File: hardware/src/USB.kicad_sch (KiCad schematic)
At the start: 0 parts

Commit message: Add: USB sheet to the schematic
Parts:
- added C301: 10nF, symbol Device:C
- added C302, C303, C304: 4.7µF, symbol Device:C
- added C305, C306, C307: 0.1µF, symbol Device:C
- added D301: SP0503BAHT, Package_TO_SOT_SMD:SOT-143, symbol Power_Protection:SP0503BAHT
- added D302, D303: LED, symbol Device:LED
- added J301: USB_C_Receptacle_USB2.0_16P, Connector_USB:USB_C_Receptacle_GCT_USB4105-xx-A_16P_TopMnt_Horizontal, symbol Connector:USB_C_Receptacle_USB2.0_16P
- added Q301, Q302: NPN, symbol Simulation_SPICE:NPN
- added R301: 0R, symbol Device:R
- added R302, R303: 5.1k, symbol Device:R
- added R304: 22.1k, symbol Device:R
- added R305: 47.5k, symbol Device:R
- added R306: 1k, symbol Device:R
- added R307, R308: 10k, symbol Device:R
- added R309, R310: 150, symbol Device:R
- added U301: CP2102N-Axx-xQFN24, Package_DFN_QFN:QFN-24-1EP_4x4mm_P0.5mm_EP2.6x2.6mm, symbol Interface_USB:CP2102N-Axx-xQFN24
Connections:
- new net: Q301.2 (B), R307.1
- new net: Q302.3 (E), R307.2, U301.19 (~{RTS})
- new net: D303.1 (K), U301.13 (~{RXT}/GPIO.1)
- new net: D303.2 (A), R310.2
- new net: Q301.3 (E), R308.2, U301.23 (~{DTR})
- new net: D302.1 (K), U301.14 (~{TXT}/GPIO.0)
- new net: D301.4 (K), J301.A6 (D+), J301.B6 (D+), U301.3 (D+)
- new net: D301.3 (K), J301.A7 (D-), J301.B7 (D-), U301.4 (D-)
- new net: R304.2, R305.1, U301.8 (VBUS)
- new net: R306.2, U301.9 (~{RST})
- new net: J301.A5 (CC1), R302.2
- new net: C301.1, J301.S1 (SHIELD), R301.1
- new net: Q302.2 (B), R308.1
- new net: J301.B5 (CC2), R303.2
- new net: D302.2 (A), R309.2
- new net +3V3: C302.1, C303.1, C304.1, C305.1, C306.1, C307.1, R306.1, R309.1, R310.1, U301.5 (VIO), U301.6 (VDD), U301.7 (VREGIN)
- new net GND: C301.2, C302.2, C303.2, C304.2, C305.2, C306.2, C307.2, D301.1 (A), J301.A1 (GND), J301.A12 (GND), J301.B1 (GND), J301.B12 (GND), R301.2, R302.1, R303.1, R305.2, U301.2 (GND), U301.25 (GND)
- new net GPIO9: Q301.1 (C)
- new net RST: Q302.1 (C)
- new net RXD: U301.20 (RXD)
- new net TXD: U301.21 (TXD)
- new net VBUS: D301.2 (K), J301.A4 (VBUS), J301.A9 (VBUS), J301.B4 (VBUS), J301.B9 (VBUS), R304.1
- no-connect marks 0 -> 8

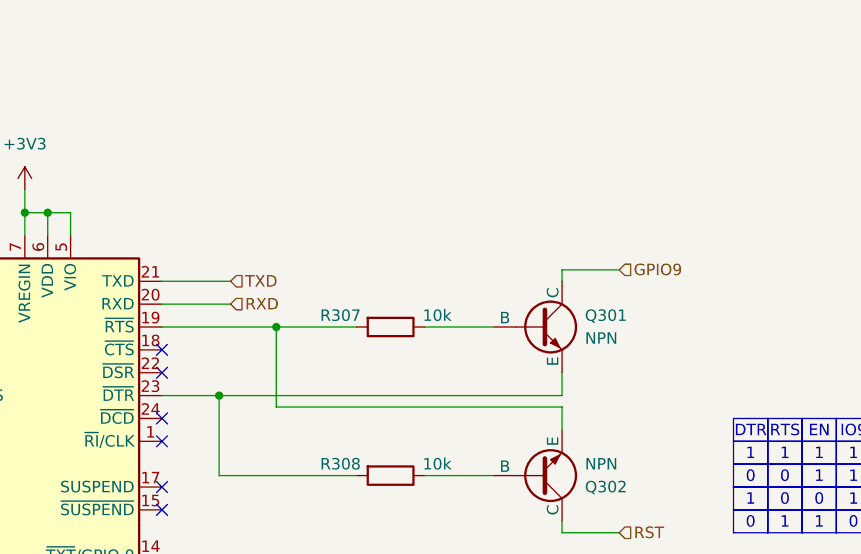
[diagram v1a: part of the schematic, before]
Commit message: Mod: Compacted the TXD and RXD into the UART bus
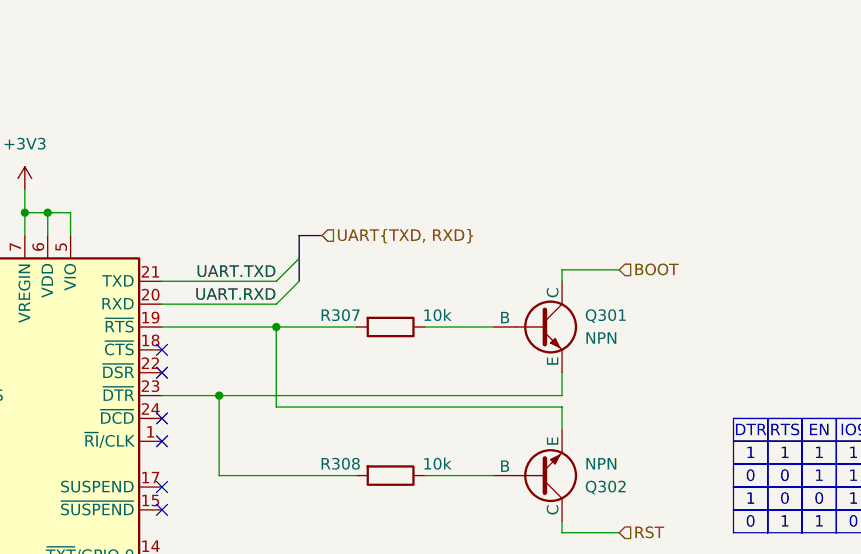
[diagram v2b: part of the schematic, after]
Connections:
- net GPIO9 renamed BOOT
- net RXD renamed UART.RXD
- net TXD renamed UART.TXD
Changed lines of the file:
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@@
 	(title_block
 		(title "Wordclock - USB")
-		(date "2024-10-19")
+		(date "2024-10-20")
 		(rev "A")
 		(company "ElektroNik Zoller")
@@
 		(at 165.1 104.14)
 	)
+	(bus_entry
+		(at 177.8 68.58)
+		(size 2.54 -2.54)
+		(stroke
+			(width 0)
+			(type default)
+		)
+	)
+	(bus_entry
+		(at 177.8 66.04)
+		(size 2.54 -2.54)
+		(stroke
+			(width 0)
+			(type default)
+		)
+	)
+	(bus
+		(pts
+			(xy 180.34 63.5) (xy 180.34 60.96)
+		)
+		(stroke
+			(width 0)
+			(type default)
+		)
+	)
 	(wire
 		(pts
@@
 	(wire
 		(pts
-			(xy 165.1 68.58) (xy 172.72 68.58)
+			(xy 165.1 68.58) (xy 177.8 68.58)
 		)
 		(stroke
@@
 		)
 	)
+	(bus
+		(pts
+			(xy 180.34 60.96) (xy 182.88 60.96)
+		)
+		(stroke
+			(width 0)
+			(type default)
+		)
+	)
 	(wire
 		(pts
@@
 	(wire
 		(pts
-			(xy 165.1 66.04) (xy 172.72 66.04)
+			(xy 165.1 66.04) (xy 177.8 66.04)
 		)
 		(stroke
@@
 		(pts
 			(xy 97.79 83.82) (xy 139.7 83.82)
+		)
+		(stroke
+			(width 0)
+			(type default)
+		)
+	)
+	(bus
+		(pts
+			(xy 180.34 66.04) (xy 180.34 63.5)
 		)
 		(stroke
@@
 		)
 	)
-	(hierarchical_label "GPIO9"
+	(label "UART.RXD"
+		(at 177.8 68.58 180)
+		(fields_autoplaced yes)
+		(effects
+			(font
+				(size 1.27 1.27)
+			)
+			(justify right bottom)
+		)
+	)
+	(label "UART.TXD"
+		(at 177.8 66.04 180)
+		(fields_autoplaced yes)
+		(effects
+			(font
+				(size 1.27 1.27)
+			)
+			(justify right bottom)
+		)
+	)
+	(hierarchical_label "BOOT"
 		(shape input)
 		(at 215.9 64.77 0)
-		(fields_autoplaced yes)
-		(effects
-			(font
-				(size 1.27 1.27)
-			)
-			(justify left)
-		)
-	)
-	(hierarchical_label "RXD"
-		(shape input)
-		(at 172.72 68.58 0)
 		(fields_autoplaced yes)
 		(effects
@@
 		)
 	)
-	(hierarchical_label "TXD"
+	(hierarchical_label "UART{TXD, RXD}"
 		(shape input)
-		(at 172.72 66.04 0)
+		(at 182.88 60.96 0)
 		(fields_autoplaced yes)
 		(effects

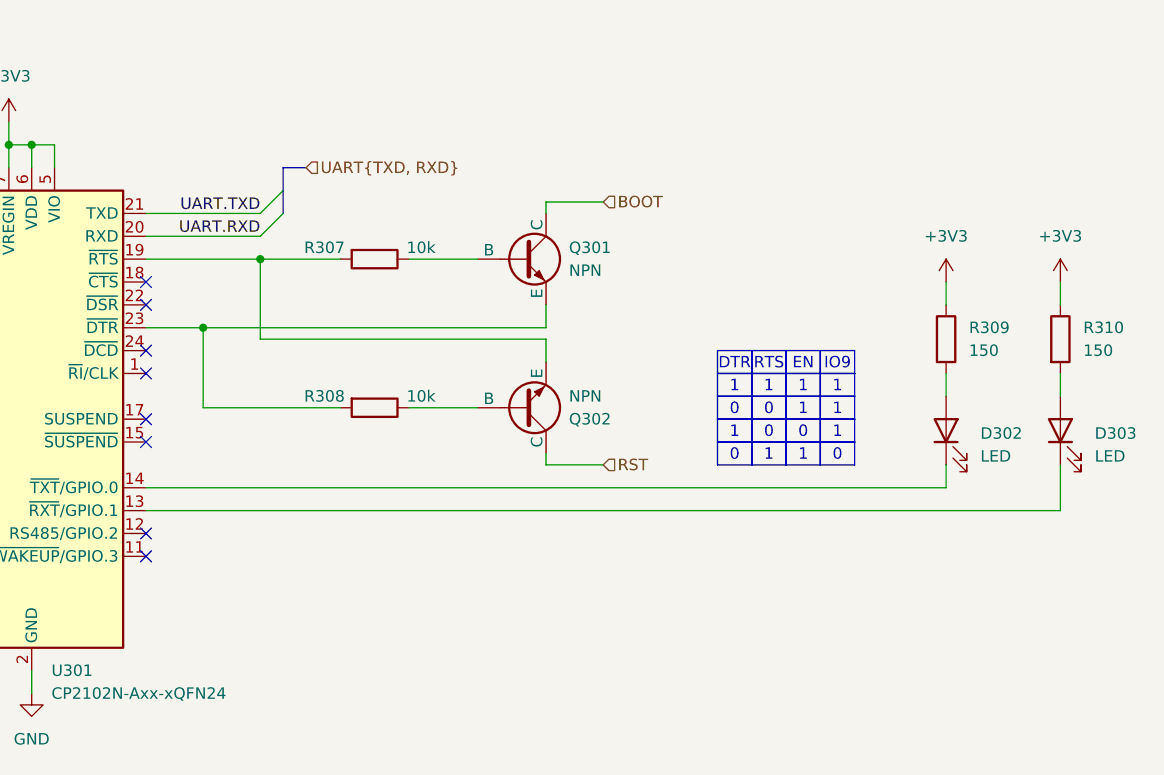
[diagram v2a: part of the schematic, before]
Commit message: Add: MCU and power supply. And connected to USB in top level schematic
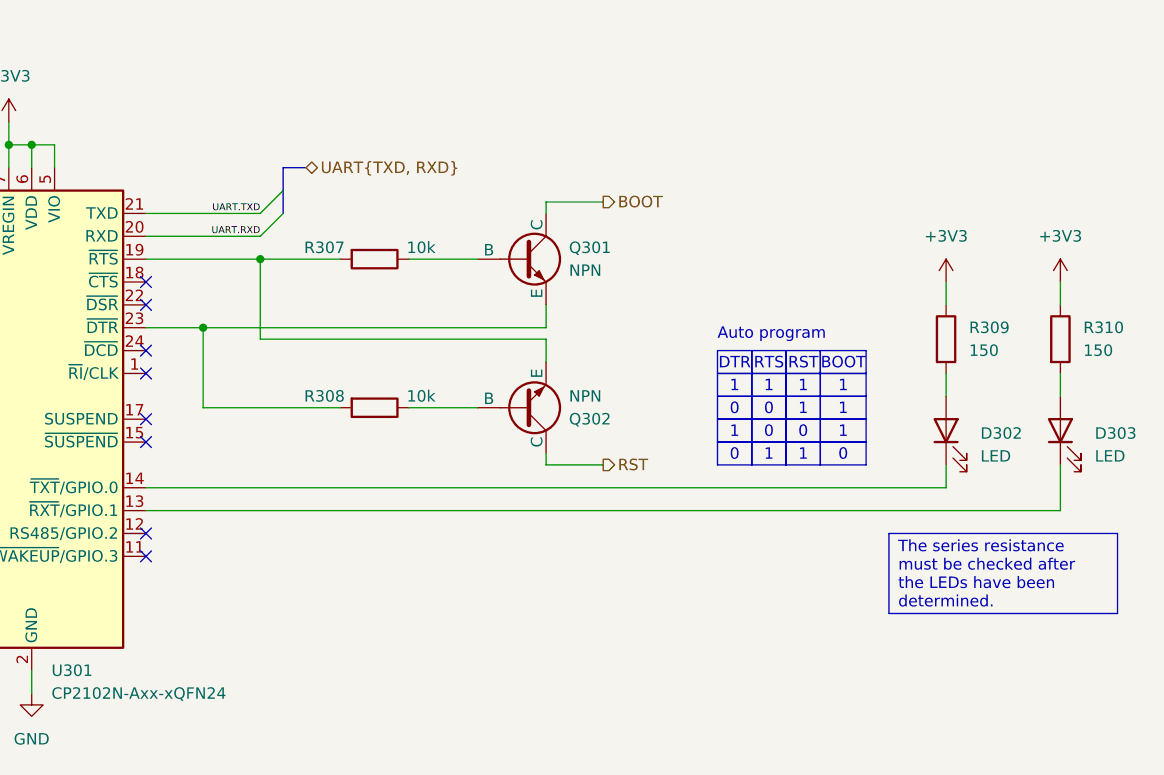
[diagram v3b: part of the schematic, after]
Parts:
- J301: Manufacturer (none) -> GCT; Manufacturer Part no. (none) -> USB4105-GF-A; Vendor 1 (none) -> Digikey; Vendor 1 Part no. (none) -> 2073-USB4105-GF-ACT-ND; Vendor 2 (none) -> LCSC; Vendor 2 Part no. (none) -> C3020560
- U301: Manufacturer (none) -> Silicon Labs; Manufacturer Part no. (none) -> CP2102N-A02-GQFN24R; Vendor 1 (none) -> Digikey; Vendor 1 Part no. (none) -> 336-5888-2-ND; Vendor 2 (none) -> LCSC; Vendor 2 Part no. (none) -> C969151
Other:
- note added: "Auto program"
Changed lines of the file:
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@@
 		(exclude_from_sim no)
 		(at 240.03 83.82 0)
-		(size 3.81 2.54)
+		(size 5.08 2.54)
+		(stroke
+			(width 0)
+			(type default)
+		)
+		(fill
+			(type none)
+		)
+		(effects
+			(font
+				(size 1.27 1.27)
+			)
+		)
+	)
+	(text_box "The series resistance must be checked after the LEDs have been determined."
+		(exclude_from_sim no)
+		(at 247.65 101.6 0)
+		(size 25.4 8.89)
 		(stroke
 			(width 0)
@@
 				(size 1.27 1.27)
 			)
+			(justify left)
 		)
 	)
@@
 		(exclude_from_sim no)
 		(at 240.03 86.36 0)
-		(size 3.81 2.54)
+		(size 5.08 2.54)
 		(stroke
 			(width 0)
@@
 		(exclude_from_sim no)
 		(at 240.03 88.9 0)
-		(size 3.81 2.54)
+		(size 5.08 2.54)
 		(stroke
 			(width 0)
@@
 		)
 	)
-	(text_box "EN"
+	(text_box "RST"
 		(exclude_from_sim no)
 		(at 236.22 81.28 0)
@@
 		(exclude_from_sim no)
 		(at 240.03 91.44 0)
-		(size 3.81 2.54)
+		(size 5.08 2.54)
 		(stroke
 			(width 0)
@@
 		)
 	)
-	(text_box "IO9"
+	(text_box "BOOT"
 		(exclude_from_sim no)
 		(at 240.03 81.28 0)
-		(size 3.81 2.54)
+		(size 5.08 2.54)
 		(stroke
 			(width 0)
@@
 		)
 	)
+	(text "Auto program"
+		(exclude_from_sim no)
+		(at 228.6 80.264 0)
+		(effects
+			(font
+				(size 1.27 1.27)
+			)
+			(justify left bottom)
+		)
+	)
 	(label "UART.RXD"
 		(at 177.8 68.58 180)
@@
 		(effects
 			(font
-				(size 1.27 1.27)
+				(size 0.762 0.762)
 			)
 			(justify right bottom)
@@
 		(effects
 			(font
-				(size 1.27 1.27)
+				(size 0.762 0.762)
 			)
 			(justify right bottom)
@@
 	)
 	(hierarchical_label "BOOT"
-		(shape input)
+		(shape output)
 		(at 215.9 64.77 0)
 		(fields_autoplaced yes)
@@
 	)
 	(hierarchical_label "RST"
-		(shape input)
+		(shape output)
 		(at 215.9 93.98 0)
 		(fields_autoplaced yes)
@@
 	)
 	(hierarchical_label "UART{TXD, RXD}"
-		(shape input)
+		(shape bidirectional)
 		(at 182.88 60.96 0)
 		(fields_autoplaced yes)
@@
 			)
 		)
+		(property "Manufacturer" "Silicon Labs"
+			(at 152.4 88.9 0)
+			(effects
+				(font
+					(size 1.27 1.27)
+				)
+				(hide yes)
+			)
+		)
+		(property "Manufacturer Part no." "CP2102N-A02-GQFN24R"
+			(at 152.4 88.9 0)
+			(effects
+				(font
+					(size 1.27 1.27)
+				)
+				(hide yes)
+			)
+		)
+		(property "Vendor 1" "Digikey"
+			(at 152.4 88.9 0)
+			(effects
+				(font
+					(size 1.27 1.27)
+				)
+				(hide yes)
+			)
+		)
+		(property "Vendor 1 Part no." "336-5888-2-ND"
+			(at 152.4 88.9 0)
+			(effects
+				(font
+					(size 1.27 1.27)
+				)
+				(hide yes)
+			)
+		)
+		(property "Vendor 2" "LCSC"
+			(at 152.4 88.9 0)
+			(effects
+				(font
+					(size 1.27 1.27)
+				)
+				(hide yes)
+			)
+		)
+		(property "Vendor 2 Part no." " C969151"
+			(at 152.4 88.9 0)
+			(effects
+				(font
+					(size 1.27 1.27)
+				)
+				(hide yes)
+			)
+		)
 		(pin "8"
 		)
@@
 			(at 50.8 81.28 0)
 			(effects
+				(font
+					(size 1.27 1.27)
+				)
+				(hide yes)
+			)
+		)
+		(property "Manufacturer" "GCT"
+			(at 50.8 81.28 0)
+			(effects
+				(font
+					(size 1.27 1.27)
+				)
+				(hide yes)
+			)
+		)
+		(property "Manufacturer Part no." "USB4105-GF-A"
+			(at 50.8 81.28 0)
+			(effects
+				(font
+					(size 1.27 1.27)
+				)
+				(hide yes)
+			)
+		)
+		(property "Vendor 1" "Digikey"
+			(at 50.8 81.28 0)
+			(effects
+				(font
+					(size 1.27 1.27)
+				)
+				(hide yes)
+			)
+		)
+		(property "Vendor 1 Part no." "2073-USB4105-GF-ACT-ND"
+			(at 50.8 81.28 0)
+			(effects
+				(font
+					(size 1.27 1.27)
+				)
+				(hide yes)
+			)
+		)
+		(property "Vendor 2" "LCSC"
+			(at 50.8 81.28 0)
+			(effects
+				(font
+					(size 1.27 1.27)
+				)
+				(hide yes)
+			)
+		)
+		(property "Vendor 2 Part no." " C3020560"
+			(at 50.8 81.28 0)
+			(effects

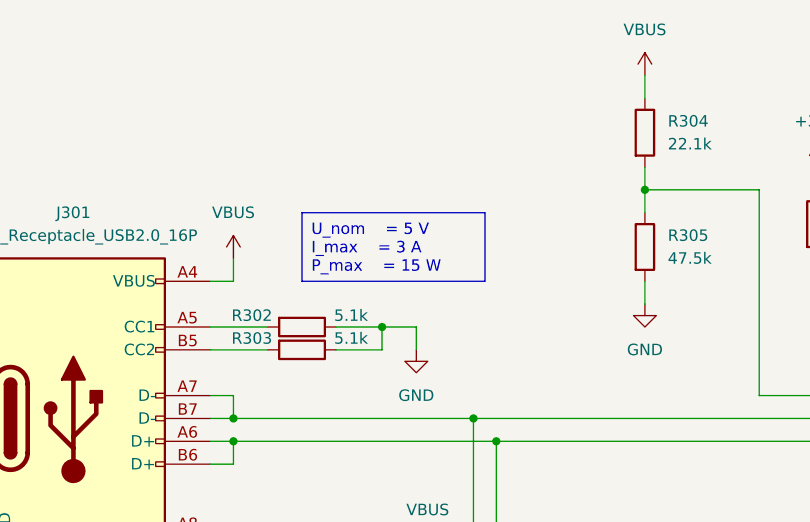
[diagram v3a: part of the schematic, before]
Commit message: Add: LEDs to the schematic
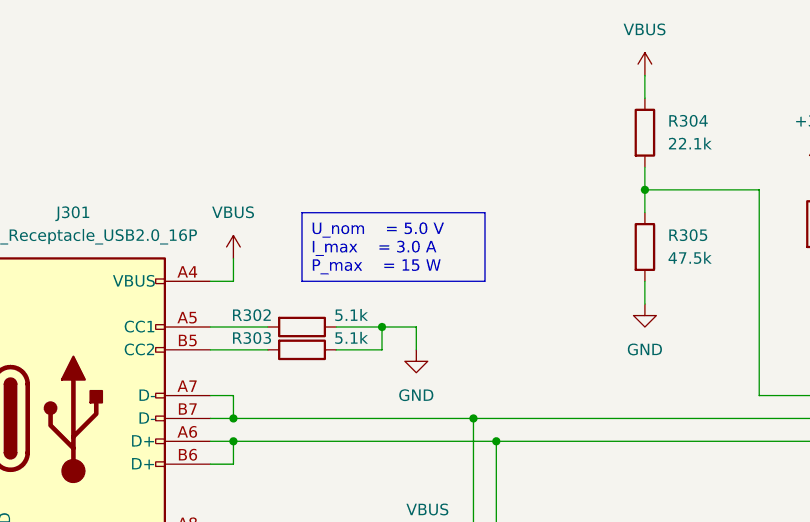
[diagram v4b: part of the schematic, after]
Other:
- title: Wordclock - USB -> Wordclock - USB & UART
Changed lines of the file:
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@@
 	(paper "A4")
 	(title_block
-		(title "Wordclock - USB")
+		(title "Wordclock - USB & UART")
 		(date "2024-10-20")
 		(rev "A")
@@
 		)
 	)
-	(text_box "U_nom	= 5 V\nI_max	= 3 A\nP_max	= 15 W"
+	(text_box "U_nom	= 5.0 V\nI_max	= 3.0 A\nP_max	= 15 W"
 		(exclude_from_sim no)
 		(at 76.2 58.42 0)

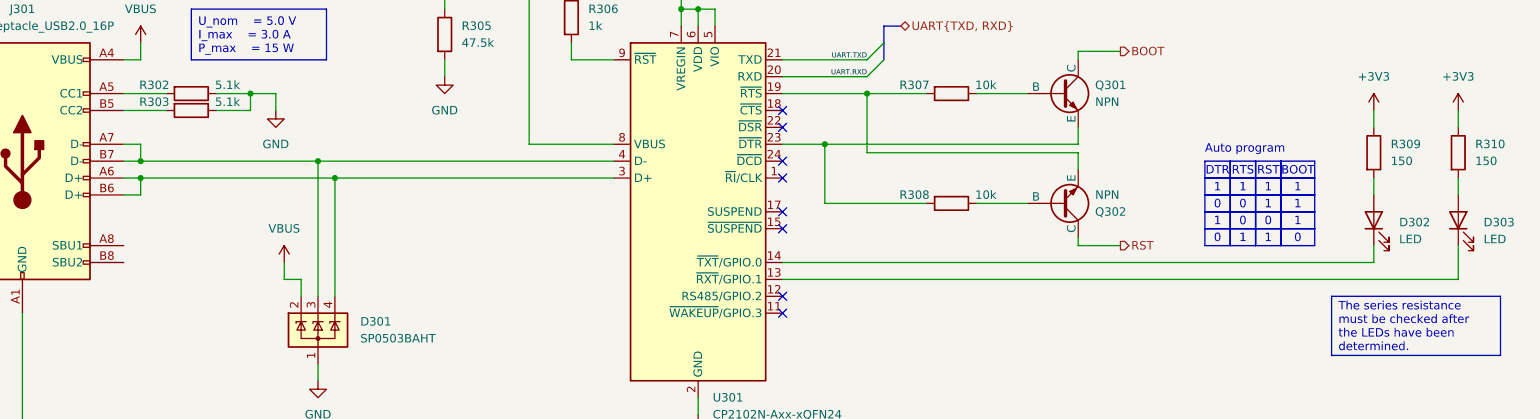
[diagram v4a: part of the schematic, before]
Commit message: Mod: RTC GPIOs
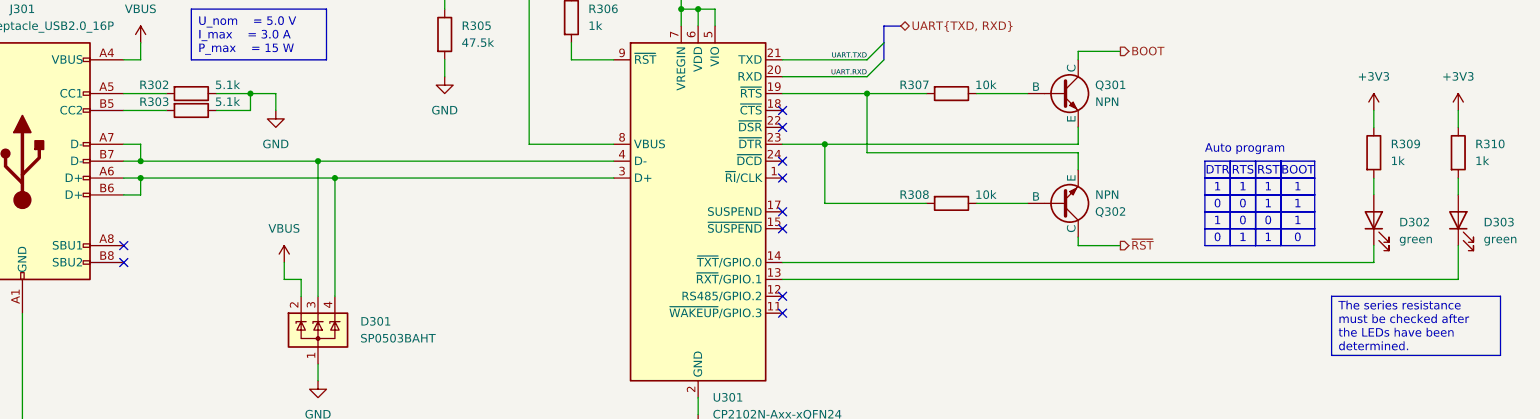
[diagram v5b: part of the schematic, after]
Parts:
- D302, D303: value LED -> green
- R309, R310: value 150 -> 1k
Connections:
- net RST renamed ~{RST}
- no-connect marks 8 -> 10
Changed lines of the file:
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@@
 	)
 	(no_connect
+		(at 66.04 93.98)
+	)
+	(no_connect
 		(at 165.1 101.6)
 	)
@@
 	)
 	(no_connect
+		(at 66.04 96.52)
+	)
+	(no_connect
 		(at 165.1 76.2)
 	)
@@
 		)
 	)
-	(hierarchical_label "RST"
+	(hierarchical_label "~{RST}"
 		(shape output)
 		(at 215.9 93.98 0)
@@
 			)
 		)
-		(property "Value" "LED"
+		(property "Value" "green"
 			(at 270.51 93.0274 90)
 			(effects
@@
 			)
 		)
-		(property "Value" "150"
+		(property "Value" "1k"
 			(at 269.24 81.2799 0)
 			(effects
@@
 			)
 		)
-		(property "Value" "LED"
+		(property "Value" "green"
 			(at 257.81 93.0274 90)
 			(effects
@@
 			)
 		)
-		(property "Value" "150"
+		(property "Value" "1k"
 			(at 256.54 81.2799 0)
 			(effects

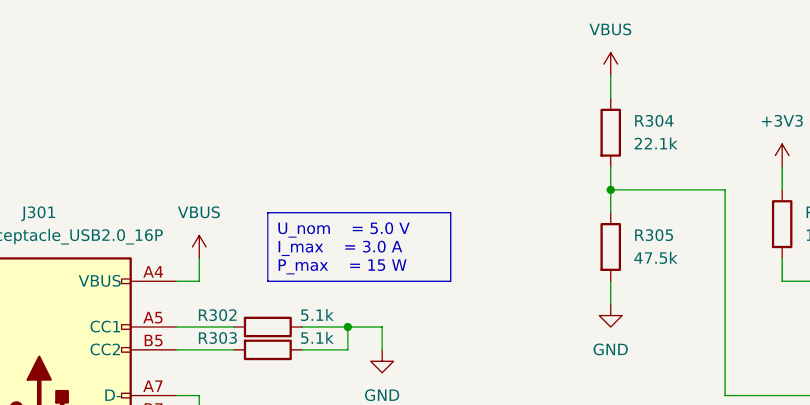
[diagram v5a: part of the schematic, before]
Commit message: Add: Level Shifter +3V3 to +5V
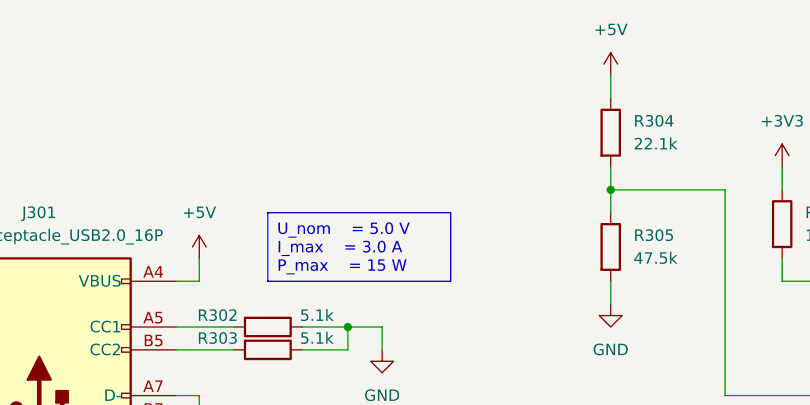
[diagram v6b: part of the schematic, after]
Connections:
- net VBUS: no longer J301.A4 (VBUS), J301.A9 (VBUS), J301.B4 (VBUS), J301.B9 (VBUS), R304.1
- new net +5V: J301.A4 (VBUS), J301.A9 (VBUS), J301.B4 (VBUS), J301.B9 (VBUS), R304.1
